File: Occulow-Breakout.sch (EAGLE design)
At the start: 18 parts

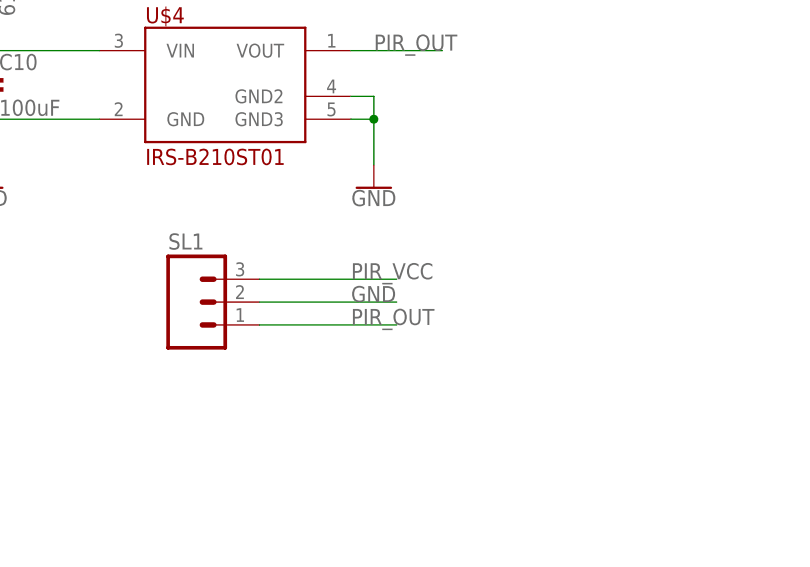
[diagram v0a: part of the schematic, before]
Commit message: IR sensor layout
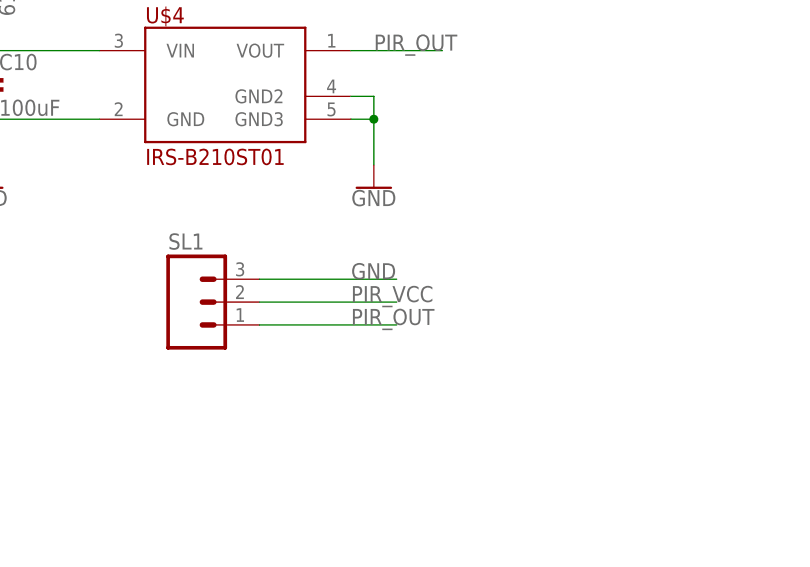
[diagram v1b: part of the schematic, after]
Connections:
- net GND: now also SL1.3; no longer SL1.2
- net PIR_VCC: now also SL1.2; no longer SL1.3
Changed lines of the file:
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@@
-</segment>
-<segment>
-<wire x1="200.66" y1="132.08" x2="215.9" y2="132.08" width="0.1524" layer="91"/>
-<label x="210.82" y="132.08" size="1.778" layer="95"/>
-<pinref part="SL1" gate="G$1" pin="2"/>
 </segment>
 <segment>
@@
 <wire x1="228.6" y1="96.52" x2="243.84" y2="96.52" width="0.1524" layer="91"/>
 <label x="233.68" y="96.52" size="1.778" layer="95"/>
+</segment>
+<segment>
+<wire x1="200.66" y1="134.62" x2="215.9" y2="134.62" width="0.1524" layer="91"/>
+<label x="210.82" y="134.62" size="1.778" layer="95"/>
+<pinref part="SL1" gate="G$1" pin="3"/>
 </segment>
 </net>
@@
 </segment>
 <segment>
-<wire x1="200.66" y1="134.62" x2="215.9" y2="134.62" width="0.1524" layer="91"/>
-<label x="210.82" y="134.62" size="1.778" layer="95"/>
-<pinref part="SL1" gate="G$1" pin="3"/>
+<wire x1="200.66" y1="132.08" x2="215.9" y2="132.08" width="0.1524" layer="91"/>
+<label x="210.82" y="132.08" size="1.778" layer="95"/>
+<pinref part="SL1" gate="G$1" pin="2"/>
 </segment>
 </net>

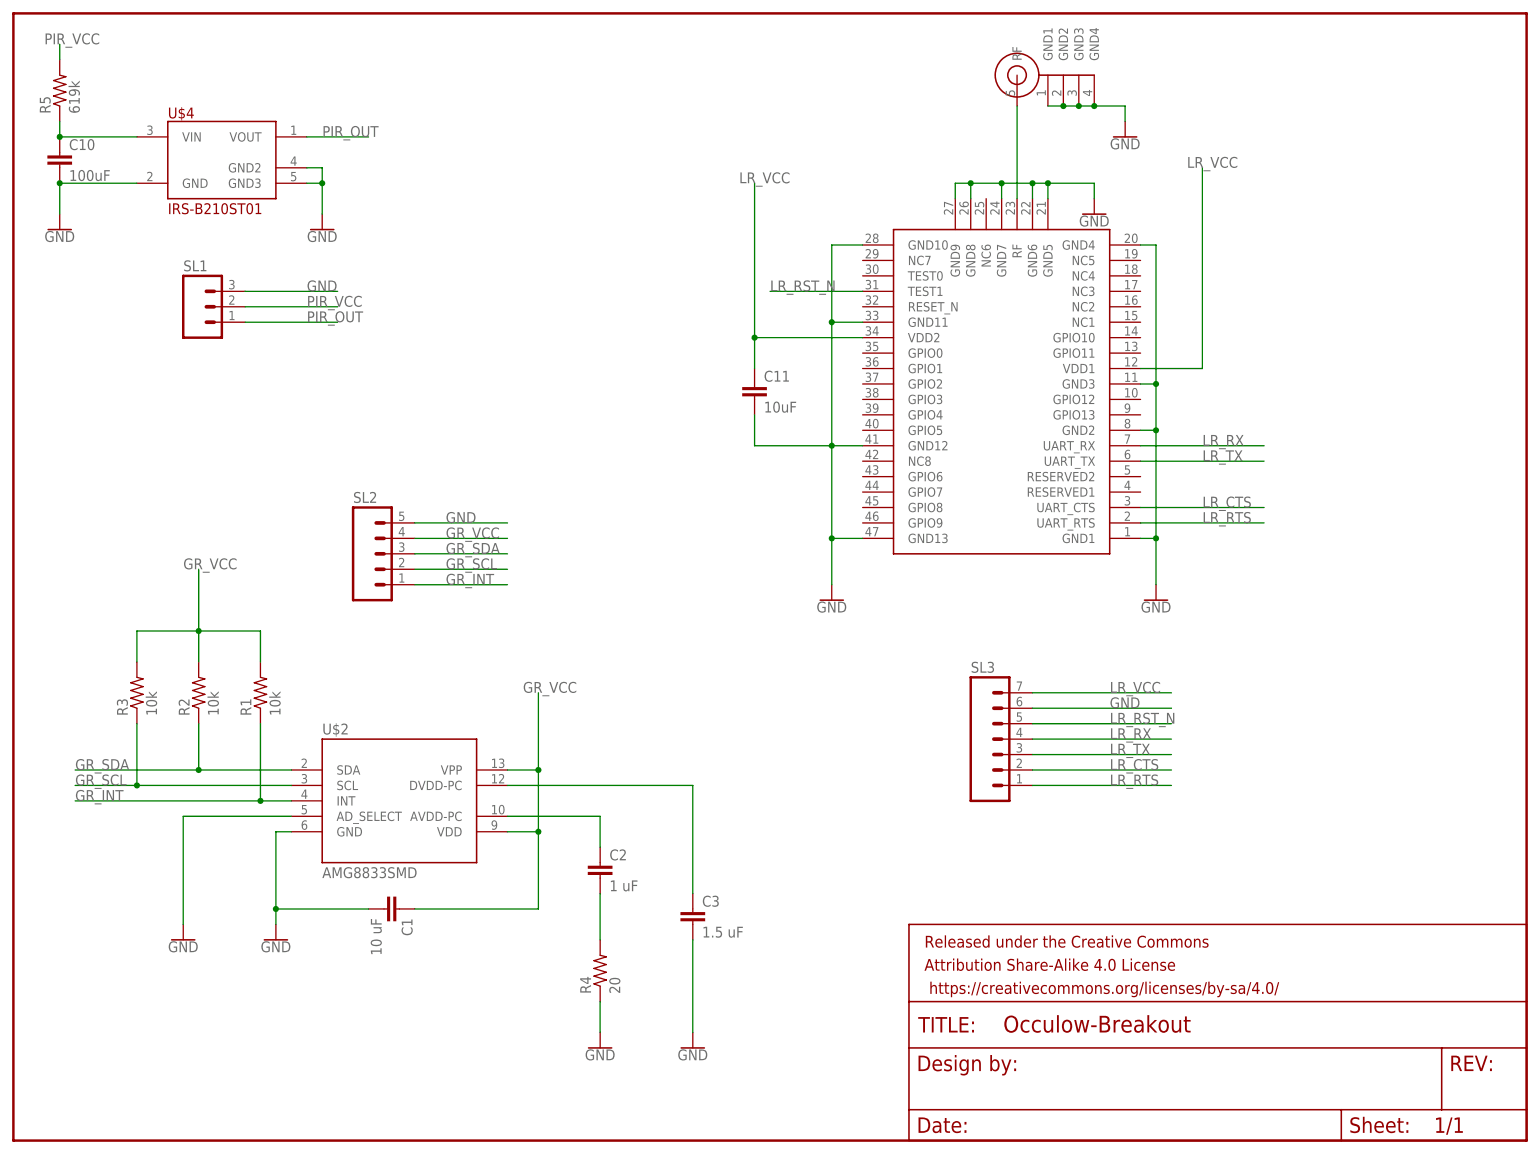
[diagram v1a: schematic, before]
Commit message: Re-named ground for each module
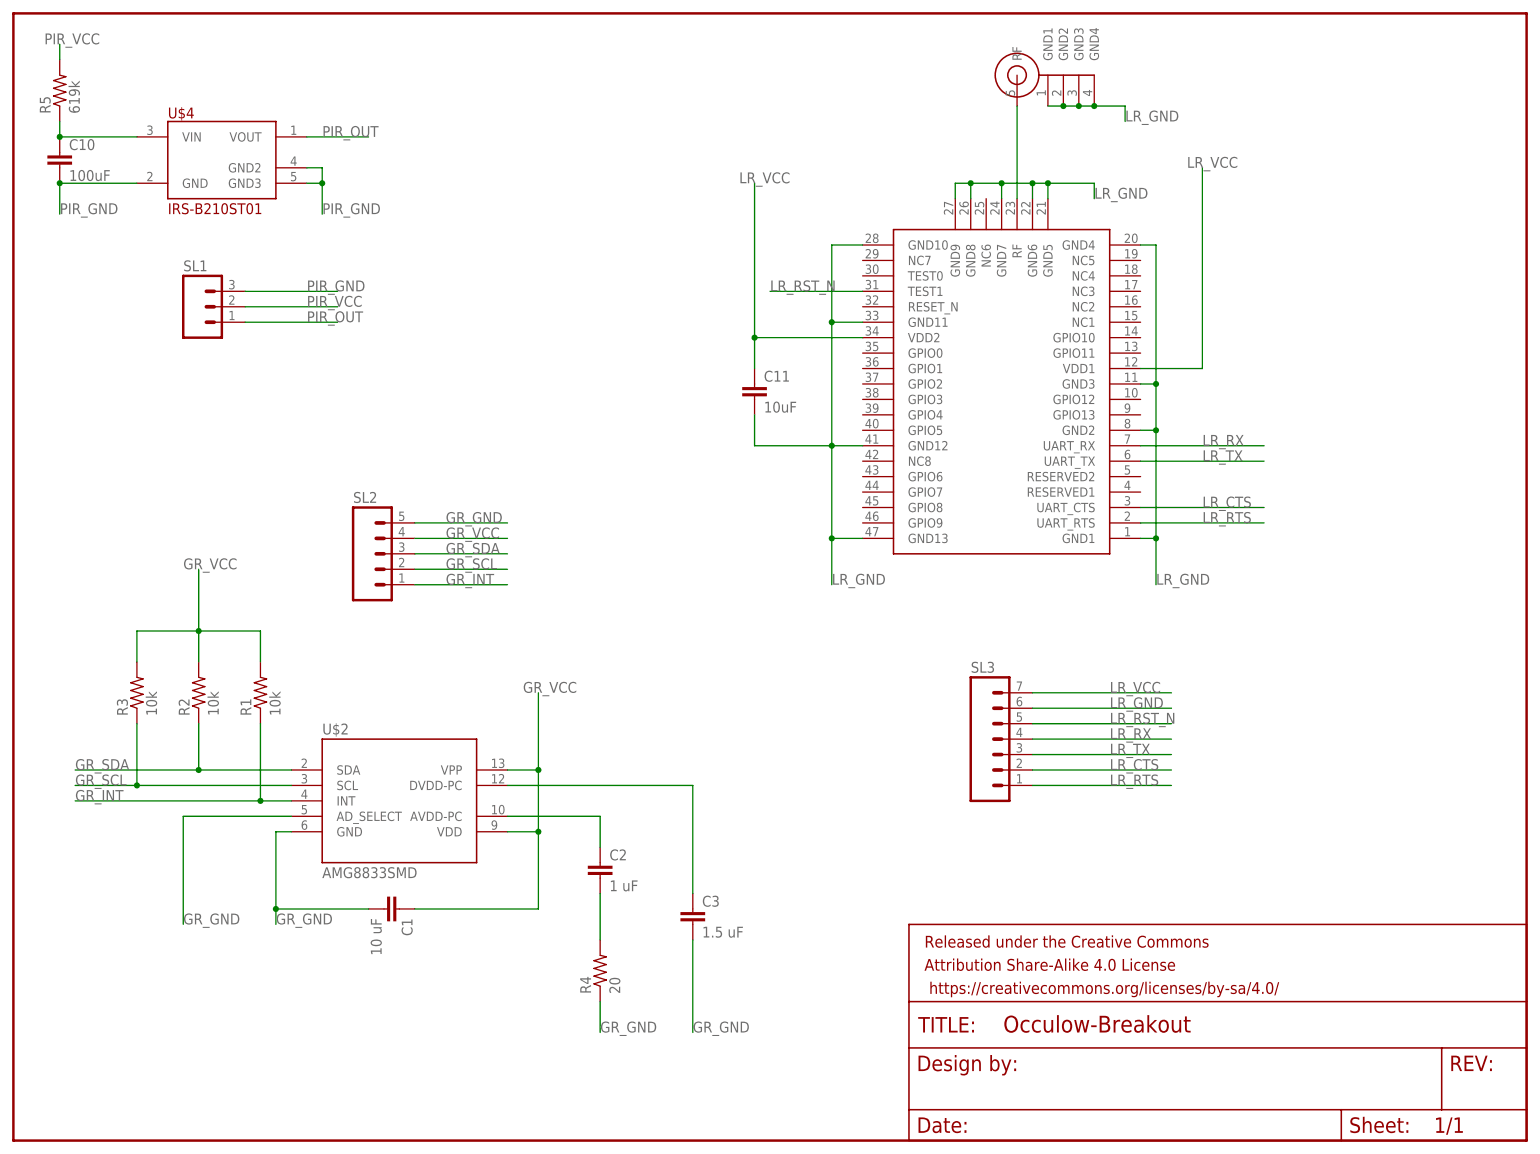
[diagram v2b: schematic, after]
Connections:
- removed net GND: C1.2, C10.2, C11.2, C3.2, R4.1, SL1.3, SL2.5, SL3.6, U$1.GND1, U$1.GND10, U$1.GND11, U$1.GND12, U$1.GND13, U$1.GND2, U$1.GND3, U$1.GND4, U$1.GND5, U$1.GND6, U$1.GND7, U$1.GND8, U$1.GND9, U$2.AD_SELECT, U$2.GND, U$3.GND1, U$3.GND2, U$3.GND3, U$3.GND4, U$4.GND, U$4.GND2, U$4.GND3
- new net GR_GND: C1.2, C3.2, R4.1, SL2.5, U$2.AD_SELECT, U$2.GND
- new net LR_GND: C11.2, SL3.6, U$1.GND1, U$1.GND10, U$1.GND11, U$1.GND12, U$1.GND13, U$1.GND2, U$1.GND3, U$1.GND4, U$1.GND5, U$1.GND6, U$1.GND7, U$1.GND8, U$1.GND9, U$3.GND1, U$3.GND2, U$3.GND3, U$3.GND4
- new net PIR_GND: C10.2, SL1.3, U$4.GND, U$4.GND2, U$4.GND3

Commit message: Rename caps, bom
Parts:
- renumbered C10 to C4, C11 to C5
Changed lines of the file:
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@@
 <?xml version="1.0" encoding="utf-8"?>
 <!DOCTYPE eagle SYSTEM "eagle.dtd">
-<eagle version="8.0.0">
+<eagle version="8.0.2">
 <drawing>
 <settings>
@@
 <part name="U$3" library="SMA-JACK" deviceset="SMA-JACK" device="FEMALE"/>
 <part name="U$4" library="PIR" deviceset="IRS-B210ST01" device=""/>
-<part name="C10" library="rcl" deviceset="C-EU" device="C1206" value="100uF"/>
+<part name="C4" library="rcl" deviceset="C-EU" device="C1206" value="100uF"/>
 <part name="R5" library="resistor" deviceset="R-US_" device="R1206" value="619k"/>
-<part name="C11" library="rcl" deviceset="C-EU" device="C1206" value="10uF"/>
+<part name="C5" library="rcl" deviceset="C-EU" device="C1206" value="10uF"/>
 <part name="SL1" library="con-amp-quick" deviceset="M03" device=""/>
 <part name="SL2" library="con-amp-quick" deviceset="M05" device=""/>
@@
 <instance part="U$3" gate="G$1" x="327.66" y="170.18"/>
 <instance part="U$4" gate="G$1" x="193.04" y="157.48"/>
-<instance part="C10" gate="G$1" x="170.18" y="157.48"/>
+<instance part="C4" gate="G$1" x="170.18" y="157.48"/>
 <instance part="R5" gate="G$1" x="170.18" y="167.64" rot="R90"/>
-<instance part="C11" gate="G$1" x="284.48" y="119.38"/>
+<instance part="C5" gate="G$1" x="284.48" y="119.38"/>
 <instance part="SL1" gate="G$1" x="193.04" y="132.08"/>
 <instance part="SL2" gate="G$1" x="220.98" y="91.44"/>
@@
 <pinref part="U$4" gate="G$1" pin="VIN"/>
 <wire x1="182.88" y1="160.02" x2="170.18" y2="160.02" width="0.1524" layer="91"/>
-<pinref part="C10" gate="G$1" pin="1"/>
+<pinref part="C4" gate="G$1" pin="1"/>
 <pinref part="R5" gate="G$1" pin="1"/>
 <wire x1="170.18" y1="160.02" x2="170.18" y2="162.56" width="0.1524" layer="91"/>
@@
 <segment>
 <pinref part="U$1" gate="G$1" pin="VDD2"/>
-<pinref part="C11" gate="G$1" pin="1"/>
+<pinref part="C5" gate="G$1" pin="1"/>
 <wire x1="302.26" y1="127" x2="284.48" y2="127" width="0.1524" layer="91"/>
 <wire x1="284.48" y1="127" x2="284.48" y2="121.92" width="0.1524" layer="91"/>
@@
 <pinref part="U$4" gate="G$1" pin="GND"/>
 <wire x1="182.88" y1="152.4" x2="170.18" y2="152.4" width="0.1524" layer="91"/>
-<pinref part="C10" gate="G$1" pin="2"/>
+<pinref part="C4" gate="G$1" pin="2"/>
 <wire x1="170.18" y1="152.4" x2="170.18" y2="147.32" width="0.1524" layer="91"/>
 <junction x="170.18" y="152.4"/>
@@
 <wire x1="302.26" y1="93.98" x2="297.18" y2="93.98" width="0.1524" layer="91"/>
 <junction x="297.18" y="93.98"/>
-<pinref part="C11" gate="G$1" pin="2"/>
+<pinref part="C5" gate="G$1" pin="2"/>
 <wire x1="284.48" y1="114.3" x2="284.48" y2="109.22" width="0.1524" layer="91"/>
 <wire x1="284.48" y1="109.22" x2="297.18" y2="109.22" width="0.1524" layer="91"/>

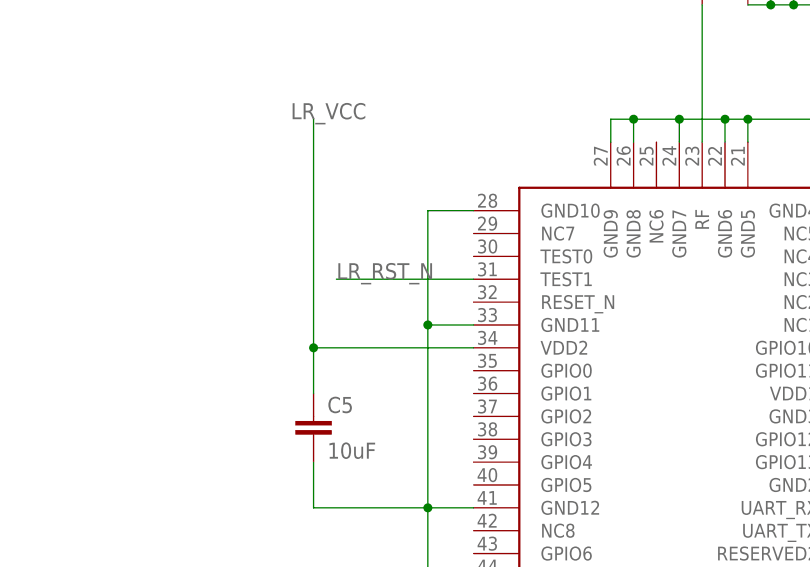
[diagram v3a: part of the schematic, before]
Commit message: Correct reset for lora
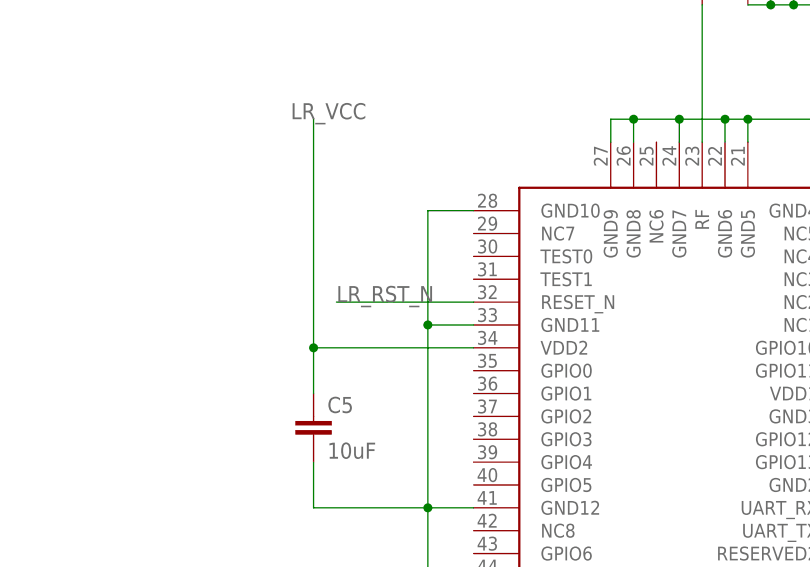
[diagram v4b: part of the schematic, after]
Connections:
- net LR_RST_N: now also U$1.RESET_N; no longer U$1.TEST1
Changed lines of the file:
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@@
 <net name="LR_RST_N" class="0">
-<segment>
-<pinref part="U$1" gate="G$1" pin="TEST1"/>
-<wire x1="302.26" y1="134.62" x2="287.02" y2="134.62" width="0.1524" layer="91"/>
-<label x="287.02" y="134.62" size="1.778" layer="95"/>
-</segment>
 <segment>
 <wire x1="330.2" y1="63.5" x2="353.06" y2="63.5" width="0.1524" layer="91"/>
@@
 <pinref part="SL3" gate="G$1" pin="5"/>
 </segment>
+<segment>
+<pinref part="U$1" gate="G$1" pin="RESET_N"/>
+<wire x1="302.26" y1="132.08" x2="287.02" y2="132.08" width="0.1524" layer="91"/>
+<label x="287.02" y="132.08" size="1.778" layer="95"/>
+</segment>
 </net>
